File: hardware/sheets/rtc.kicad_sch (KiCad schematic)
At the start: 9 parts, among them U1 DS12C887, U2 74HCT138, U3 74HCT02, U4 74HCT08, U5 74HCT32, U6 74HCT04

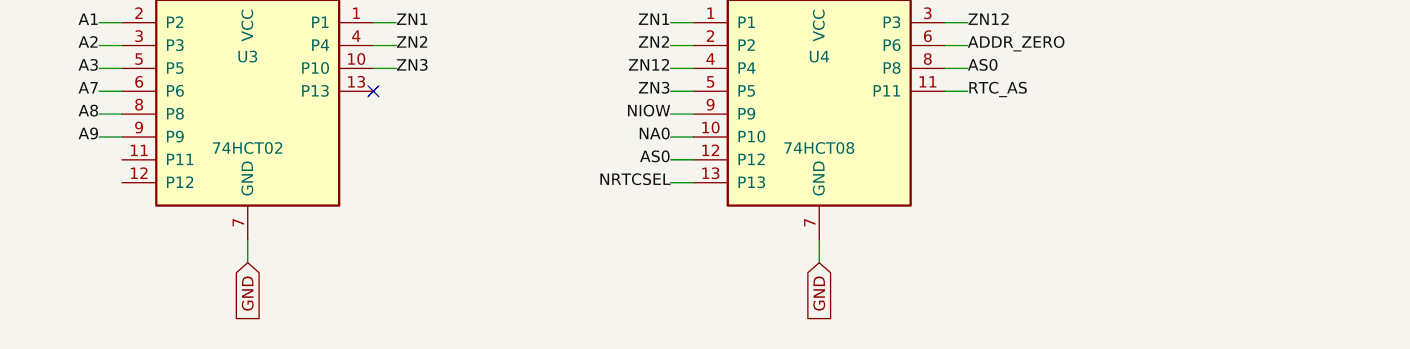
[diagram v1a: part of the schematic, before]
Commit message: Fix all low-severity + toolchain design-review findings
Low:
- LPT IRQ7 via tri-state '125 (NAND-enabled ack pulse) - shareable line
- card_com JP2 IRQ strap follows the base-address strap (was IRQ4-only)
- Supervisor USB-A VBUS fused (500mA polyfuse)
- card_isatest: DUT_PWR_EN moved to the control '595 (addr shifts can't
  glitch DUT power); '165s -> 74HC grade (HCT needs VCC 4.5-5.5V)
- /3 duty comments corrected; U13 marked load-bearing inverting buffer
- RTC AS hold-path bench note; duplicate ~RD stub removed
- mxbus PRIV_DECODE emptied (Y5 never leaves cpu_core)

Toolchain:
- build.py/build_cards return real exit codes, failing on structural ERC
  (endpoint_off_grid/unconnected_wire_endpoint/multiple_net_names) or a
  failed netlist export
- KiCad paths resolved via mxsch.kicad_cli()/kicad_symdir() (env, PATH,
  snap `current`) - no pinned snap revision anywhere
- Deterministic UUIDs (uuid5 title-seed + counter): rebuilds are
  byte-identical (verified); this rewrites every UUID once
- S-expression string escapes now round-trip (parse decodes, dump encodes)
- CLAUDE.md updated to match

The new structural gate immediately caught its own batch's bug (pull row
placed inside card_isatest's J2 pin field) - moved and re-verified.

Co-Authored-By: Claude Fable 5 <noreply@anthropic.com>
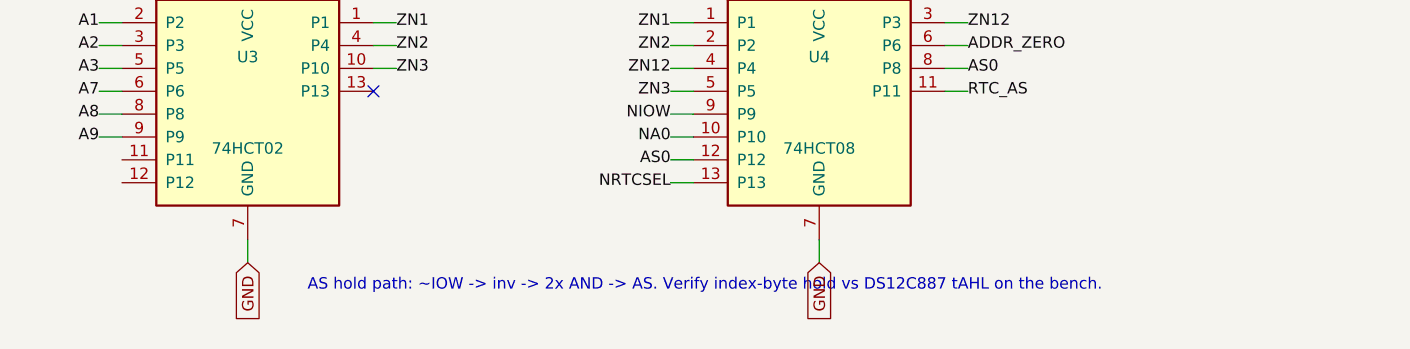
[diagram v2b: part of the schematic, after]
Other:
- note added: "AS hold path: ~IOW -> inv -> 2x AND -> AS. Verify index-byte hold vs DS12C887 tAHL on the bench."
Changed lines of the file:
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@@
+		)
+	)
+	(text "AS hold path: ~IOW -> inv -> 2x AND -> AS. Verify index-byte hold vs DS12C887 tAHL on the bench."
+		(at 139.7 236.22 0)
+		(effects
+			(font
+				(size 1.27 1.27)
+			)
 		)
 	)
@@
 		(instances
 			(project "mini-xt"
-				(path "/9d1a32b9-fdc3-4ebf-878d-e57919a1b88e/fb6d58d6-f9fb-4009-8de7-b9037a118d75"
+				(path "/26736c46-8b40-5460-874f-03596d17270c/f7cab9cf-eafa-5d8f-bb87-e538548d1944"
 					(reference "U801")
 					(unit 1)
@@
 		(instances
 			(project "mini-xt"
-				(path "/9d1a32b9-fdc3-4ebf-878d-e57919a1b88e/fb6d58d6-f9fb-4009-8de7-b9037a118d75"
+				(path "/26736c46-8b40-5460-874f-03596d17270c/f7cab9cf-eafa-5d8f-bb87-e538548d1944"
 					(reference "R801")
 					(unit 1)
@@
 		(instances
 			(project "mini-xt"
-				(path "/9d1a32b9-fdc3-4ebf-878d-e57919a1b88e/fb6d58d6-f9fb-4009-8de7-b9037a118d75"
+				(path "/26736c46-8b40-5460-874f-03596d17270c/f7cab9cf-eafa-5d8f-bb87-e538548d1944"
 					(reference "U802")
 					(unit 1)
@@
 		(instances
 			(project "mini-xt"
-				(path "/9d1a32b9-fdc3-4ebf-878d-e57919a1b88e/fb6d58d6-f9fb-4009-8de7-b9037a118d75"
+				(path "/26736c46-8b40-5460-874f-03596d17270c/f7cab9cf-eafa-5d8f-bb87-e538548d1944"
 					(reference "U803")
 					(unit 1)
@@
 		(instances
 			(project "mini-xt"
-				(path "/9d1a32b9-fdc3-4ebf-878d-e57919a1b88e/fb6d58d6-f9fb-4009-8de7-b9037a118d75"
+				(path "/26736c46-8b40-5460-874f-03596d17270c/f7cab9cf-eafa-5d8f-bb87-e538548d1944"
 					(reference "U804")
 					(unit 1)
@@
 		(instances
 			(project "mini-xt"
-				(path "/9d1a32b9-fdc3-4ebf-878d-e57919a1b88e/fb6d58d6-f9fb-4009-8de7-b9037a118d75"
+				(path "/26736c46-8b40-5460-874f-03596d17270c/f7cab9cf-eafa-5d8f-bb87-e538548d1944"
 					(reference "U805")
 					(unit 1)
@@
 		(instances
 			(project "mini-xt"
-				(path "/9d1a32b9-fdc3-4ebf-878d-e57919a1b88e/fb6d58d6-f9fb-4009-8de7-b9037a118d75"
+				(path "/26736c46-8b40-5460-874f-03596d17270c/f7cab9cf-eafa-5d8f-bb87-e538548d1944"
 					(reference "U806")
 					(unit 1)
@@
 		(instances
 			(project "mini-xt"
-				(path "/9d1a32b9-fdc3-4ebf-878d-e57919a1b88e/fb6d58d6-f9fb-4009-8de7-b9037a118d75"
+				(path "/26736c46-8b40-5460-874f-03596d17270c/f7cab9cf-eafa-5d8f-bb87-e538548d1944"
 					(reference "C801")
 					(unit 1)
@@
 		(instances
 			(project "mini-xt"
-				(path "/9d1a32b9-fdc3-4ebf-878d-e57919a1b88e/fb6d58d6-f9fb-4009-8de7-b9037a118d75"
+				(path "/26736c46-8b40-5460-874f-03596d17270c/f7cab9cf-eafa-5d8f-bb87-e538548d1944"
 					(reference "C802")
 					(unit 1)

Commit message: JLCPCB sourcing pass: verify pinouts, LCSC part numbers, SMD build
Custom-symbol verification (open-questions Q5 resolved):
- MAX3241 symbol was wrong on nearly every pin and used MAX3243-style
  control names; regenerated to the real SSOP-28 pinout (SHDN#/EN#/
  R1OUTB/R2OUTB) and com_port rewired -- EN# must be GROUNDED (the old
  ~FORCEON-high would have disabled the receivers on real silicon)
- DS12C887 symbol wrong on 4 pins (DS=17, RESET#=18, IRQ#=19, SQW=23)

Sourcing (every part checked against the JLC DB; ~45 line items):
- New tools/parts.py maps (lib_id, value) -> LCSC; build.py applies it as
  an 'LCSC Part Num' property on every component (384 across the project)
- Sheets stay generic; stock-forced substitutions bound in the map:
  '374->'574 (parallel rewired), '163->'161, '157->HC157 (+HCT-buffered
  3.3V selects, I0/I1 swapped), '02->HC02, TCM809->MCP809, 2N3904->MMBT3904
- bus_mcu address counters moved to the 3.3V domain (HC161 on 3V3_BUS,
  loaded from MCU-side MD0-7; HCT244s read the 3.3V outputs at TTL Vih)
- 14.318 XOs are 3.3V-only parts: powered from 3V3, squared up via spare
  HCT gates (cpu_core U13, card_isatest U19)
- COM baud reference is now a 1.8432MHz crystal on the 16C550's XIN/XOUT
  (3.3V-only oscillators vs a 5V-only soft card)
- Supervisor QSPI header replaced with a real W25Q128JVSIQ
- Socket policy (fab installs sockets): V20 DIP-40, SRAM DIP-32 (no 5V
  512Kx8 SRAM at JLC at all), DS12C887 DIP-24, female headers for modules

Docs: CLAUDE.md fabrication-constraints section (SMD, 100x100mm, generic-
symbols rule, voltage-domain rule); README + hardware/README fab notes;
notes/jlcpcb-sourcing.md (decisions, thin-stock flags, not-at-JLC list);
stale questions-sidecar.md collapsed to its supersession record.

Rebuilt motherboard + cards: structural ERC 0, byte-identical rebuilds.

Co-Authored-By: Claude Fable 5 <noreply@anthropic.com>
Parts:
- C1, C2: LCSC Part Num (none) -> C14663
- R1: LCSC Part Num (none) -> C25804
- U1: LCSC Part Num (none) -> C72120
- U2: LCSC Part Num (none) -> C5965
- U3: value 74HCT02 -> 74HC02; LCSC Part Num (none) -> C5588
- U4: LCSC Part Num (none) -> C5959
- U5: LCSC Part Num (none) -> C5985
- U6: LCSC Part Num (none) -> C672096
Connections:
- net RTC_DS: now also U1.17 (DS); no longer U1.16 (DS)
- net RTC_IRQ_L: now also U1.19 (~{IRQ}); no longer U1.18 (~{IRQ})
- net RTC_RST_L: now also U1.18 (~{RESET}); no longer U1.17 (~{RESET})
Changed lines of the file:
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@@
+			)
+		)
+		(property "LCSC Part Num" "C72120"
+			(at 228.6 116.84 0)
+			(effects
+				(font
+					(size 1.27 1.27)
+				)
+				(hide yes)
 			)
 		)
@@
 		(pin "14"
 		)
-		(pin "16"
+		(pin "17"
 		)
 		(pin "15"
@@
 		(pin "13"
 		)
-		(pin "17"
-		)
 		(pin "18"
 		)
-		(pin "21"
+		(pin "19"
+		)
+		(pin "23"
 		)
 		(pin "1"
@@
 			)
 		)
+		(property "LCSC Part Num" "C25804"
+			(at 254 88.9 0)
+			(effects
+				(font
+					(size 1.27 1.27)
+				)
+				(hide yes)
+			)
+		)
 		(pin "1"
 		)
@@
 			)
 		)
+		(property "LCSC Part Num" "C5965"
+			(at 88.9 81.28 0)
+			(effects
+				(font
+					(size 1.27 1.27)
+				)
+				(hide yes)
+			)
+		)
 		(pin "1"
 		)
@@
 			)
 		)
-		(property "Value" "74HCT02"
+		(property "Value" "74HC02"
 			(at 88.9 220.98 0)
 			(effects
@@
 		)
 		(property "Footprint" ""
+			(at 88.9 215.9 0)
+			(effects
+				(font
+					(size 1.27 1.27)
+				)
+				(hide yes)
+			)
+		)
+		(property "LCSC Part Num" "C5588"
 			(at 88.9 215.9 0)
 			(effects
@@
 			)
 		)
+		(property "LCSC Part Num" "C5959"
+			(at 152.4 215.9 0)
+			(effects
+				(font
+					(size 1.27 1.27)
+				)
+				(hide yes)
+			)
+		)
 		(pin "1"
 		)
@@
 			)
 		)
+		(property "LCSC Part Num" "C5985"
+			(at 152.4 160.02 0)
+			(effects
+				(font
+					(size 1.27 1.27)
+				)
+				(hide yes)
+			)
+		)
 		(pin "1"
 		)
@@
 			)
 		)
+		(property "LCSC Part Num" "C672096"
+			(at 88.9 160.02 0)
+			(effects
+				(font
+					(size 1.27 1.27)
+				)
+				(hide yes)
+			)
+		)
 		(pin "1"
 		)
@@
 			)
 		)
+		(property "LCSC Part Num" "C14663"
+			(at 228.6 175.26 0)
+			(effects
+				(font
+					(size 1.27 1.27)
+				)
+				(hide yes)
+			)
+		)
 		(pin "1"
 		)
@@
 			(at 152.4 96.52 0)
 			(effects
+				(font
+					(size 1.27 1.27)
+				)
+				(hide yes)
+			)
+		)
+		(property "LCSC Part Num" "C14663"
+			(at 152.4 96.52 0)
+			(effects

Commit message: Swap DIP sockets to machined-pin versions
V20 DIP-40 -> C2874018, SRAM DIP-32 x2 -> C2874017, DS12C887 DIP-24 ->
C2684765 (all round-hole/machined, verified 600 mil row spacing).
Better grip and repeated-insertion tolerance for the vintage chips;
~$2.50/board-set over stamped tin. Stamped fallbacks noted in
jlcpcb-sourcing.md.

Co-Authored-By: Claude Fable 5 <noreply@anthropic.com>
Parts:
- U1: LCSC Part Num C72120 -> C2684765
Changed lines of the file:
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@@
 			)
 		)
-		(property "LCSC Part Num" "C72120"
+		(property "LCSC Part Num" "C2684765"
 			(at 228.6 116.84 0)
 			(effects

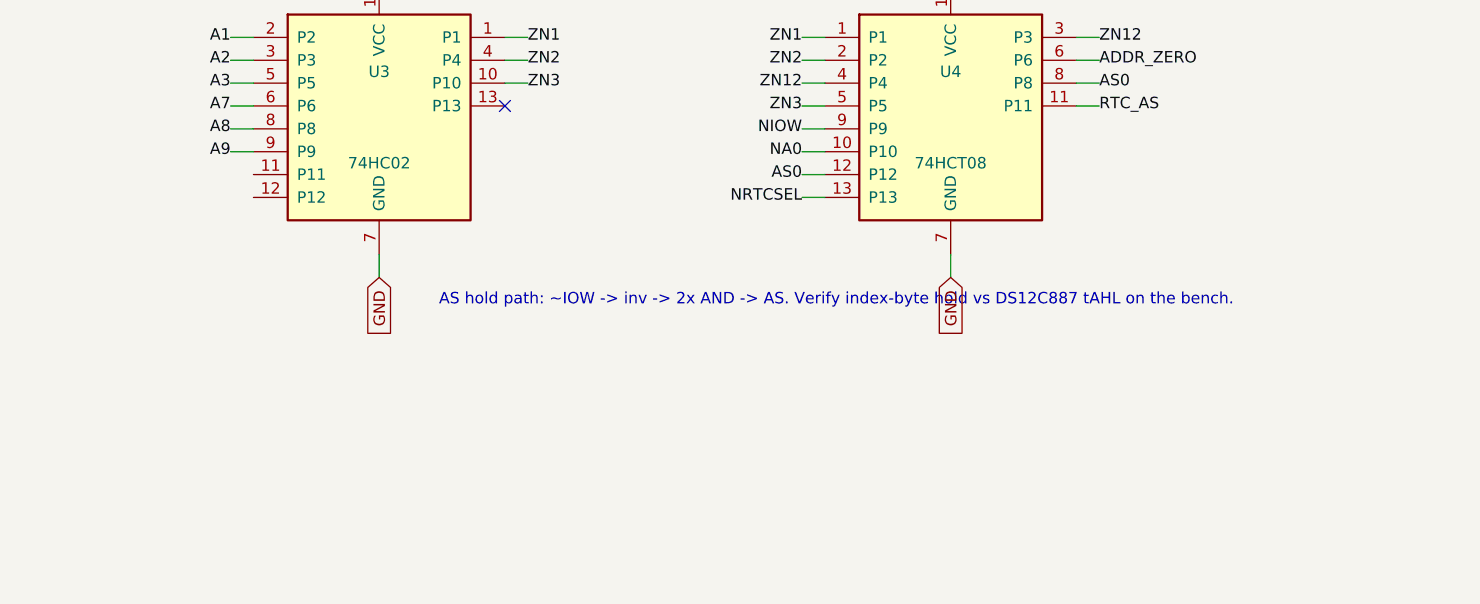
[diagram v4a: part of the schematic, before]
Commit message: Design review 2026-07-11: rail protection, decoupling, wiring fixes
Protection:
- Sidecar +5V now feeds through a 2A polyfuse into +5V_ISA with an
  SMBJ5.0A clamp + 22uF bulk (a faulted ISA card trips its own fuse
  instead of dropping the board; back-fed voltage is clamped).
- USB-C VBUS enters through a 3A polyfuse with an SMBJ5.0A on +5V
  (backstop for the CFG1 9-20V failure mode). CH224K gains a 1uF VDD
  cap; its PG routes to Supervisor GPIO16 as PD_PG. Buck output
  doubled to 2x22uF, 10uF at VIN, extra rail bulk.
- Supervisor USB-A host port: 27R series termination (RP2040
  requirement), USBLC6-2SC6 ESD array, 100uF VBUS bulk.
- Video: HDMI +5V fused (500mA), HPD sensed on GPIO41, 100R series on
  VGA sync. TMDS ESD array deferred to layout (no symbol).
- card_isatest: V5RAW bulk, Q1 gate soft-start cap, TVS on DUT rail.

Wiring fixes:
- SPKR had no driver anywhere (netlist: 1 node). Bus MCU GPIO22
  reassigned from the diagnostics-only bus-CLK sense to SPKR; bus_mcu
  drops CLK from its interface. Doc 5.2 updated.
- bus_mcu C8 decoupled +3V3, a rail that sheet never uses -> 3V3_BUS.
- Storage IRQ5 was push-pull (permanently driven when idle) -> 2N7002
  + gated '125 tri-state, same convention as the LPT IRQ7 stage.
- MAX3241 pump caps resized to the 5V datasheet values (47nF/330nF).
- LPT DB25 status inputs get 4.7k pull-ups (floated with no printer).
- Audio line-out gets a 100R series isolator before the jack.

Best practices:
- Decoupling to ~1x100nF per IC on every sheet + bulk per board
  (cpu_core 7->16 incl. the naked 3.3V oscillator, storage 4->11,
  parallel 6->13, rtc/com/video/bus_mcu/card_isatest similar).
- All floating spare CMOS inputs tied ('00/'74/'157/'02/'04/'125
  sections across cpu_core, bus_mcu, rtc, storage, card_isatest).

Sourcing: new parts mapped in parts.py with JLC-verified LCSC numbers;
Power_Protection lib registered in the tools; TPS563200 stock alert
(4 pcs left at JLC) flagged in parts.py + jlcpcb-sourcing.md. All
decisi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
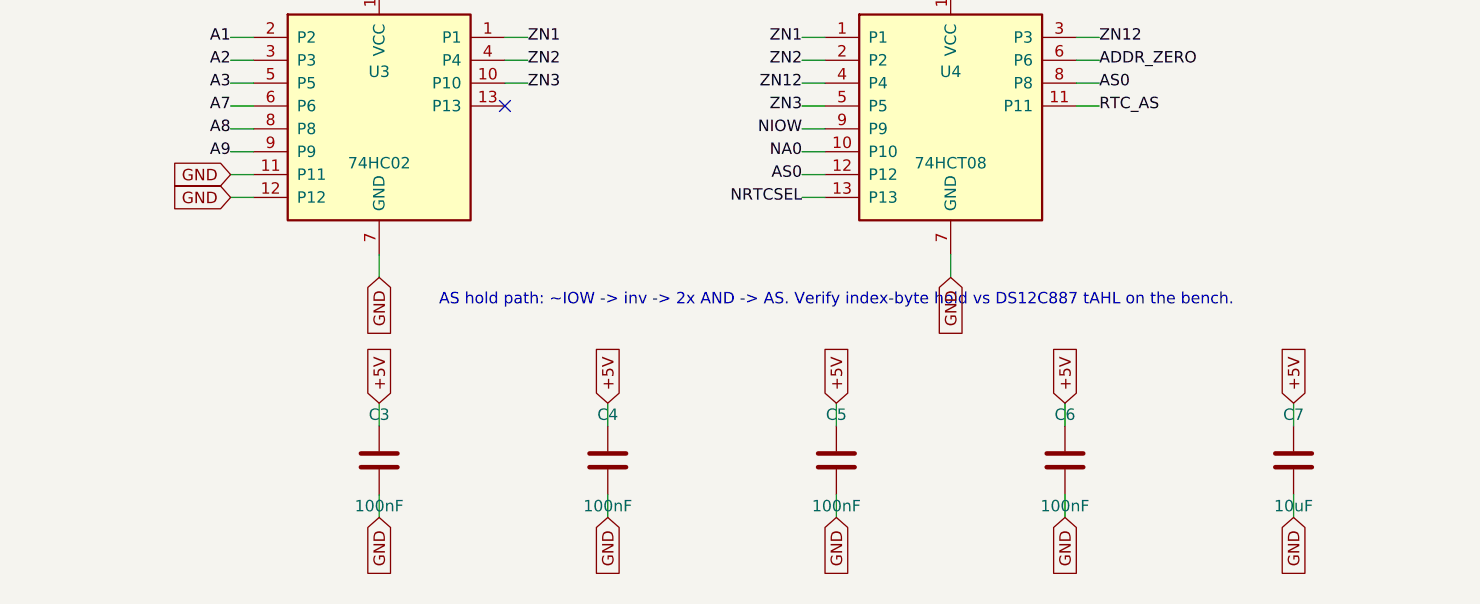
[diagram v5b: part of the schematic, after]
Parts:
- added C3, C4, C5, C6: 100nF, symbol Device:C
- added C7: 10uF, symbol Device:C
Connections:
- net +5V: now also C3.1, C4.1, C5.1, C6.1, C7.1
- net GND: now also U3.11 (P11), U3.12 (P12), C3.2, C4.2, C5.2, C6.2, C7.2
